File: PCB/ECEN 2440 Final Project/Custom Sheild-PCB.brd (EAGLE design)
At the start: 58.4 x 102.9 mm, 19 parts

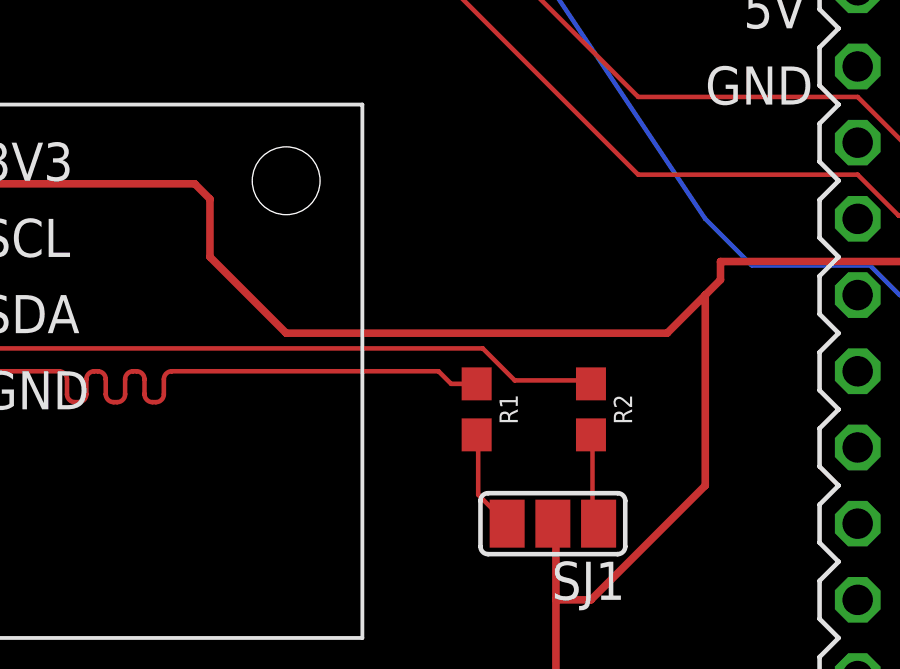
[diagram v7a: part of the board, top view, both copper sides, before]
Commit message: Created PWM code and did stuff with code
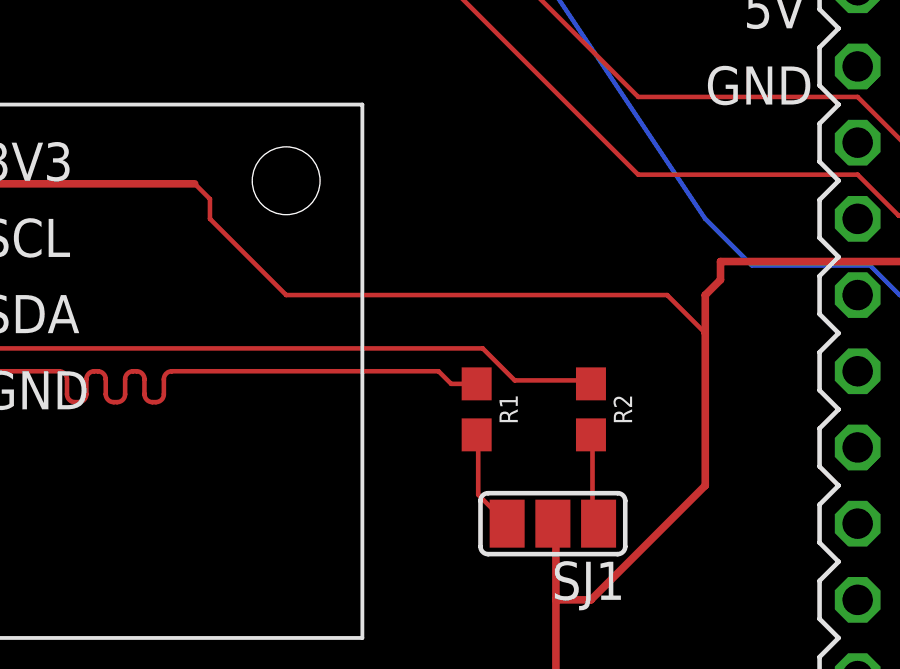
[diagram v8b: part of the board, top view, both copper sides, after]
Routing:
- net +3V3: track 118.9 -> 117.6 mm
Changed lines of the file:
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@@
 <wire x1="44.958" y1="41.148" x2="44.958" y2="41.7576" width="0.254" layer="1"/>
 <wire x1="40.64" y1="30.48" x2="39.4716" y2="30.48" width="0.254" layer="1"/>
-<wire x1="27.432" y1="44.3484" x2="27.94" y2="43.8404" width="0.254" layer="1"/>
-<wire x1="27.94" y1="43.8404" x2="27.94" y2="41.91" width="0.254" layer="1"/>
-<wire x1="27.94" y1="41.91" x2="30.48" y2="39.37" width="0.254" layer="1"/>
-<wire x1="30.48" y1="39.37" x2="43.18" y2="39.37" width="0.254" layer="1"/>
-<wire x1="43.18" y1="39.37" x2="44.45" y2="40.64" width="0.254" layer="1"/>
 <wire x1="44.45" y1="40.64" x2="44.958" y2="41.148" width="0.254" layer="1"/>
-<wire x1="44.45" y1="40.64" x2="44.45" y2="34.29" width="0.254" layer="1"/>
+<wire x1="44.45" y1="40.64" x2="44.45" y2="39.37" width="0.254" layer="1"/>
+<wire x1="44.45" y1="39.37" x2="44.45" y2="34.29" width="0.254" layer="1"/>
 <wire x1="44.45" y1="34.29" x2="40.64" y2="30.48" width="0.254" layer="1"/>
 <wire x1="22.86" y1="20.32" x2="24.13" y2="21.59" width="0.254" layer="1"/>
@@
 <wire x1="25.4" y1="24.13" x2="29.21" y2="24.13" width="0.254" layer="1"/>
 <wire x1="29.21" y1="24.13" x2="29.21" y2="23.9776" width="0.254" layer="1"/>
+<wire x1="27.432" y1="44.3484" x2="27.94" y2="43.8404" width="0.1524" layer="1"/>
+<wire x1="27.94" y1="43.8404" x2="27.94" y2="43.18" width="0.1524" layer="1"/>
+<wire x1="27.94" y1="43.18" x2="30.48" y2="40.64" width="0.1524" layer="1"/>
+<wire x1="43.18" y1="40.64" x2="44.45" y2="39.37" width="0.1524" layer="1"/>
+<wire x1="30.48" y1="40.64" x2="43.18" y2="40.64" width="0.1524" layer="1"/>
 </signal>
 <signal name="SD_CD1">
